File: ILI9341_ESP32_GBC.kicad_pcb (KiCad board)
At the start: 2 copper layers, 70 x 122.2 mm, 149 parts, among them CN2 PJ-3043-B, J1 USB_C_Receptacle_USB2.0_16P, J5 Micro_SD_Card_CD, J6 Conn_01x18_Socket, J7 Conn_01x32, Q10 XYC-PT204B-L1, Q2 BC817, Q3 BC817, Q5 PMOS, Q6 BC817, Q7 PMOS, Q8 PMOS, SW10 SW_Push, SW11 SW_Push, SW12 SW_Push, SW2 SW_Push, SW3 SW_Push, SW4 SW_Push, SW5 SW_Push, SW6 K3-1290S-J1, SW7 SW_Push, SW8 SW_Push, SW9 SW_Push, U1 CH340N, U11 ESP32-WROVER-E-N8R8, U2 XM5062S, U3 HT2348ARTZ8, U4 BQ25171QWDRCRQ1, U5 MCP23017_SO, U6 MCP23017_SO, U7 02FVS3, U8 PAM8406D, U9 TPS61028DRCR

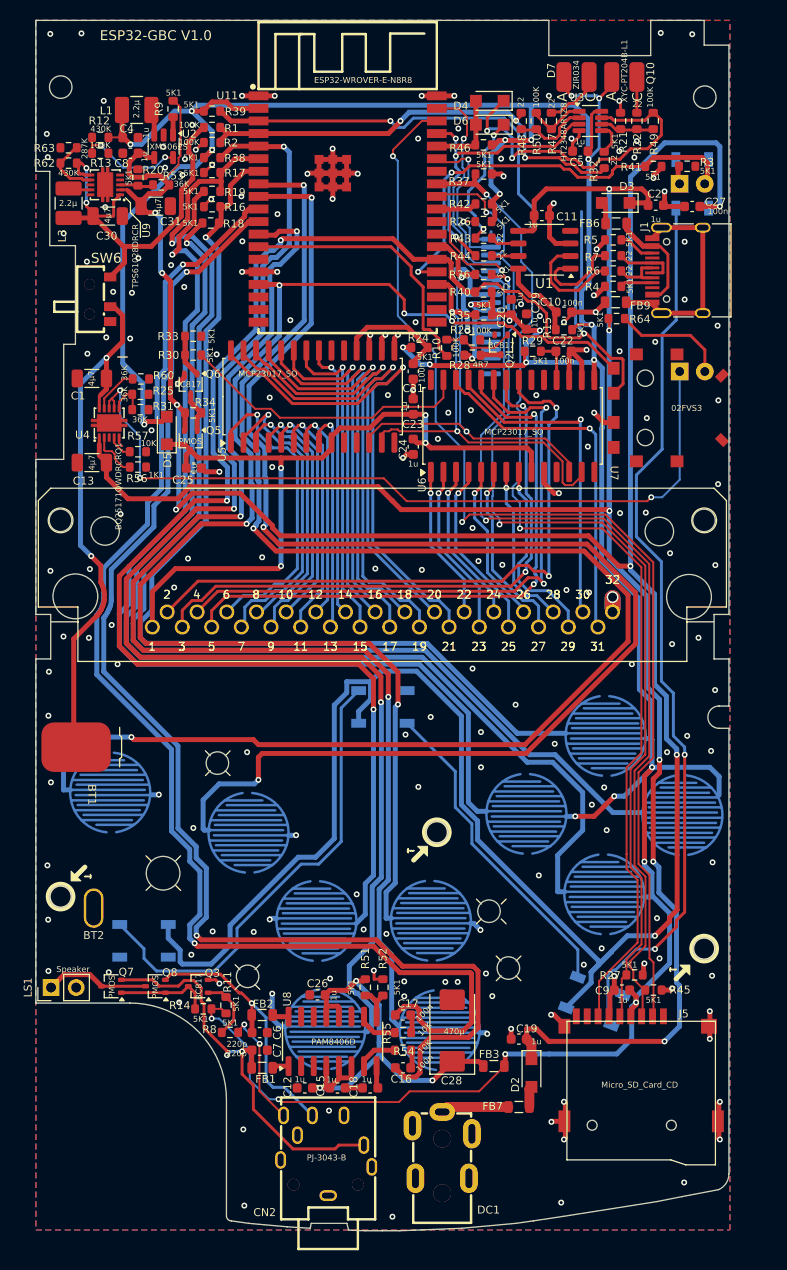
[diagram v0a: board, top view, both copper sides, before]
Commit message: update online version before change to esp32 s3
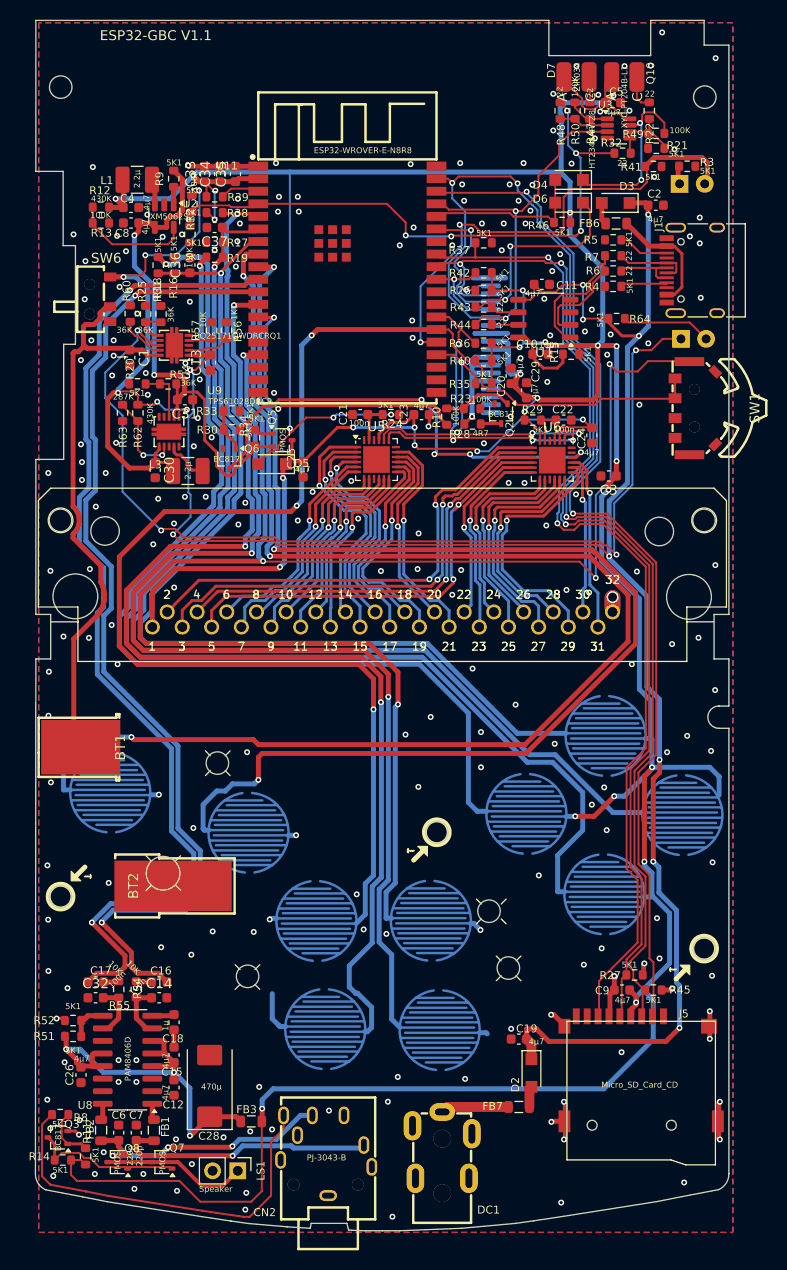
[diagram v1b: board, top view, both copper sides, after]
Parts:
- removed C27: 100n, Capacitor_SMD:C_0603_1608Metric
- removed D10, D11, D8, D9: WS2812B, LED_SMD:LED_WS2812B_PLCC4_5.0x5.0mm_P3.2mm
- removed FB9: FerriteBead_Small, Inductor_SMD:L_0805_2012Metric
- removed U7: 02FVS3, TheBrutzlers_Lib:02FVS3
- added C14: 220p, Capacitor_SMD:C_0603_1608Metric, F.Cu at (119.9, 135.8)
- added C3: 4µ7, Capacitor_SMD:C_0603_1608Metric, F.Cu at (165.3, 83.1)
- added C32: 220p, Capacitor_SMD:C_0603_1608Metric, F.Cu at (113.5, 135.8)
- added C33: 4µ7, Capacitor_SMD:C_0603_1608Metric, F.Cu at (124.5, 52.6)
- added C34: 4µ7, Capacitor_SMD:C_0603_1608Metric, F.Cu at (126.0, 52.6)
- added C35: 4µ7, Capacitor_SMD:C_0603_1608Metric, F.Cu at (127.6, 52.6)
- added C36: 220p, Capacitor_SMD:C_0603_1608Metric, F.Cu at (123.0, 61.8)
- added C37: 220p, Capacitor_SMD:C_0603_1608Metric, F.Cu at (125.5, 58.0)
- added SW1: TM-2023, easyeda2kicad:SW-SMD_TM-2023-1, F.Cu at (174.0, 76.2)
- BT1: footprint TheBrutzlers_Lib:BATTERY_AA_SMD_PLUS -> easyeda2kicad:CONN-SMD_MY-ZJ-3030
- BT2: footprint TheBrutzlers_Lib:NINTENDO_MINUS -> easyeda2kicad:BAT-SMD_MY-FJ-3031
- C1, C13, C30, C31: footprint Capacitor_SMD:C_1206_3216Metric -> Capacitor_SMD:C_0603_1608Metric
- C11, C12, C15, C19, C2, C20, C23, C24, C25, C26, C29, C4, C5, C8, C9: value 1u -> 4µ7
- C18: value 1u -> 1µ
- U5, U6: value MCP23017_SO -> AW9523B; footprint Package_SO:SOIC-28W_7.5x17.9mm_P1.27mm -> Package_DFN_QFN:QFN-24-1EP_4x4mm_P0.5mm_EP2.7x2.7mm
- moved R52 31.5 mm to (111.2, 138.1), turned to 180 degrees
- moved C17 31.2 mm to (113.5, 134.2)
- moved R51 29.9 mm to (111.2, 139.7), turned to 0 degrees
- moved L3 29.6 mm to (122.8, 82.6), turned to 0 degrees
- moved R55 29.0 mm to (115.8, 135.0), turned to -90 degrees
- moved R54 27.6 mm to (117.6, 135.0), turned to -90 degrees
- moved R63 27.3 mm to (116.2, 76.7), turned to -90 degrees
- moved LS1 26.4 mm to (127.8, 153.3), turned to -90 degrees
- moved R62 26.2 mm to (117.8, 76.7), turned to -90 degrees
- moved C16 26.1 mm to (119.9, 134.2), turned to 180 degrees
- moved C30 26.1 mm to (119.5, 82.5), turned to -90 degrees
- moved U9 25.7 mm to (120.9, 78.6), turned to -90 degrees
- moved C26 25.2 mm to (112.0, 143.6), turned to -90 degrees
- moved FB3 25.1 mm to (129.2, 148.3)
- moved C28 25.1 mm to (125.0, 144.7)
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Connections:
- C21 pad 2: Net-(U5-~{RESET}) -> Net-(U5-~{RST})
- C22 pad 2: Net-(U6-~{RESET}) -> Net-(U6-~{RST})
- J1 pad A1: Net-(J1-SHIELD) -> GND
- J1 pad A12: Net-(J1-SHIELD) -> GND
- J1 pad B1: Net-(J1-SHIELD) -> GND
- J1 pad B12: Net-(J1-SHIELD) -> GND
- J1 pad S1: Net-(J1-SHIELD) -> GND
- R24 pad 2: Net-(U5-~{RESET}) -> Net-(U5-~{RST})
- R29 pad 2: Net-(U6-~{RESET}) -> Net-(U6-~{RST})
- R30 pad 1: Net-(U6-GPA6) -> Net-(U6-P1_6)
- U5 pad 1: /DMG_CARD/CARD_A0 -> /DMG_CARD/CARD_A8
- U5 pad 10: GND -> /DMG_CARD/CARD_A4
- U5 pad 11: unconnected-(U5-NC-Pad11) -> /DMG_CARD/CARD_A5
- U5 pad 12: /I2C_CLK -> /DMG_CARD/CARD_A6
- U5 pad 13: /I2C_SDA -> /DMG_CARD/CARD_A7
- U5 pad 14: unconnected-(U5-NC-Pad14) -> /DMG_CARD/CARD_A12
- U5 pad 15: GND -> /DMG_CARD/CARD_A13
- U5 pad 16: GND -> /DMG_CARD/CARD_A14
- U5 pad 17: GND -> /DMG_CARD/CARD_A15
- U5 pad 18: Net-(U5-~{RESET}) -> GND
- U5 pad 19: unconnected-(U5-INTB-Pad19) -> /I2C_CLK
- U5 pad 2: /DMG_CARD/CARD_A1 -> /DMG_CARD/CARD_A9
- U5 pad 20: unconnected-(U5-INTA-Pad20) -> /I2C_SDA
- U5 pad 21: /DMG_CARD/CARD_A8 -> /DMG_CARD/CARD_VCC
- U5 pad 22: /DMG_CARD/CARD_A9 -> unconnected-(U5-~{INT}-Pad22)
- U5 pad 23: /DMG_CARD/CARD_A10 -> Net-(U5-~{RST})
- U5 pad 24: /DMG_CARD/CARD_A11 -> GND
- U5 pad 25: /DMG_CARD/CARD_A12 -> GND
- U5 pad 3: /DMG_CARD/CARD_A2 -> /DMG_CARD/CARD_A10
- U5 pad 4: /DMG_CARD/CARD_A3 -> /DMG_CARD/CARD_A11
- U5 pad 5: /DMG_CARD/CARD_A4 -> /DMG_CARD/CARD_A0
- U5 pad 6: /DMG_CARD/CARD_A5 -> /DMG_CARD/CARD_A1
- U5 pad 7: /DMG_CARD/CARD_A6 -> /DMG_CARD/CARD_A2
- U5 pad 8: /DMG_CARD/CARD_A7 -> /DMG_CARD/CARD_A3
- U5 pad 9: /DMG_CARD/CARD_VCC -> GND
- U6 pad 1: /DMG_CARD/CARD_D0 -> /DMG_CARD/CARD_CLK
- U6 pad 10: GND -> /DMG_CARD/CARD_D4
- U6 pad 11: unconnected-(U6-NC-Pad11) -> /DMG_CARD/CARD_D5
- U6 pad 12: /I2C_CLK -> /DMG_CARD/CARD_D6
- U6 pad 13: /I2C_SDA -> /DMG_CARD/CARD_D7
- U6 pad 14: unconnected-(U6-NC-Pad14) -> /DMG_CARD/CARD_~{RES}
- U6 pad 15: +3V3 -> /DMG_CARD/CARD_VIN
- U6 pad 16: GND -> Net-(U6-P1_6)
- U6 pad 17: GND -> unconnected-(U6-P1_7-Pad17)
- U6 pad 18: Net-(U6-~{RESET}) -> GND
- U6 pad 19: unconnected-(U6-INTB-Pad19) -> /I2C_CLK
- U6 pad 2: /DMG_CARD/CARD_D1 -> /DMG_CARD/CARD_~{WR}
- U6 pad 20: unconnected-(U6-INTA-Pad20) -> /I2C_SDA
- U6 pad 21: /DMG_CARD/CARD_CLK -> /DMG_CARD/CARD_VCC
- U6 pad 22: /DMG_CARD/CARD_~{WR} -> unconnected-(U6-~{INT}-Pad22)
- U6 pad 23: /DMG_CARD/CARD_~{RD} -> Net-(U6-~{RST})
- U6 pad 24: /DMG_CARD/CARD_~{CS} -> +3V3
- U6 pad 25: /DMG_CARD/CARD_~{RES} -> GND
- U6 pad 3: /DMG_CARD/CARD_D2 -> /DMG_CARD/CARD_~{RD}
- U6 pad 4: /DMG_CARD/CARD_D3 -> /DMG_CARD/CARD_~{CS}
- U6 pad 5: /DMG_CARD/CARD_D4 -> /DMG_CARD/CARD_D0
- U6 pad 6: /DMG_CARD/CARD_D5 -> /DMG_CARD/CARD_D1
- U6 pad 7: /DMG_CARD/CARD_D6 -> /DMG_CARD/CARD_D2
- U6 pad 8: /DMG_CARD/CARD_D7 -> /DMG_CARD/CARD_D3
- U6 pad 9: /DMG_CARD/CARD_VCC -> GND
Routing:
- net /V_BOOST: track 318.5 -> 53.2 mm, vias 8 -> 2
- net Net-(D8-DOUT): track 90.9 -> 0.00 mm, vias 2 -> 0
- net GND: track 138.1 -> 48.1 mm, vias 185 -> 216
- net Net-(D10-DOUT): track 47.5 -> 0.00 mm
- net Net-(U6-P1_6): track 0.00 -> 42.1 mm, vias 0 -> 4
- net /EN: track 40.4 -> 4.04 mm, vias 1 -> 0
- net Net-(D10-DIN): track 32.8 -> 0.00 mm
- net /SOUND_LEFT: track 132.8 -> 102.0 mm
- net /DMG_CARD/CARD_A15: track 53.1 -> 22.8 mm
- net Net-(U6-GPA6): track 29.7 -> 0.00 mm
- net /SPK_nEN: track 11.9 -> 39.9 mm, vias 2 -> 0
- net /SOUND_RIGHT: track 131.7 -> 103.7 mm
- net /DMG_CARD/CARD_A14: track 47.6 -> 19.6 mm
- net +3V3: track 371.6 -> 395.1 mm, vias 27 -> 25
- net /DMG_CARD/CARD_A13: track 47.1 -> 23.8 mm
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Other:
- outline, holes or cut-outs redrawn
- board text added: "ESP32-GBC V1.1"
- board text removed: "ESP32-GBC V1.0"

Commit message: updated version with esp32 s3 and i2s audio ic
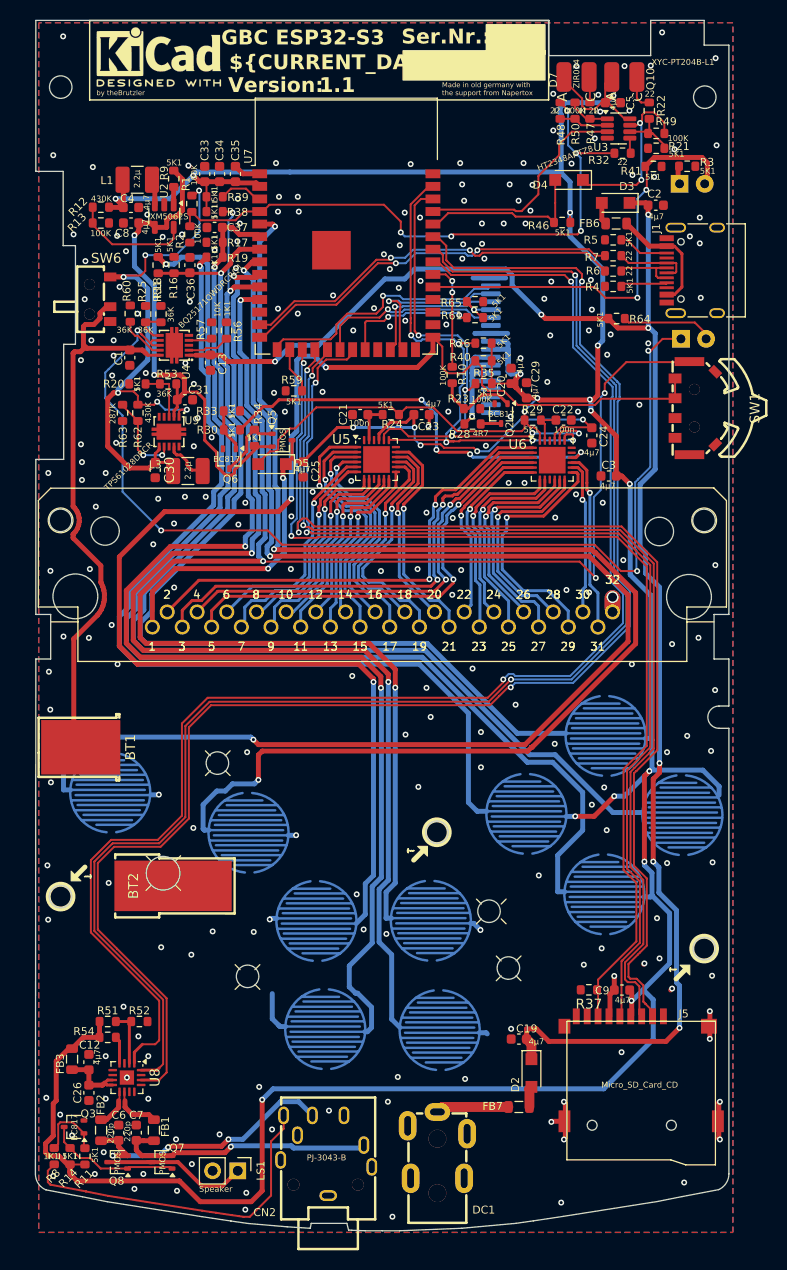
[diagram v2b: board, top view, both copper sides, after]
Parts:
- removed C10, C16, C17: 100n, Capacitor_SMD:C_0603_1608Metric
- removed C11, C15: 4µ7, Capacitor_SMD:C_0603_1608Metric
- removed C14, C32: 220p, Capacitor_SMD:C_0603_1608Metric
- removed C18: 1µ, Capacitor_SMD:C_0603_1608Metric
- removed C28: 470µ, Capacitor_Tantalum_SMD:CP_EIA-7343-43_Kemet-X
- removed D6: D, Diode_SMD:Nexperia_CFP3_SOD-123W
- removed R15, R26, R27, R42, R45: 5K1, Resistor_SMD:R_0603_1608Metric
- removed R43, R44: 22, Resistor_SMD:R_0603_1608Metric
- removed R55: 10K, Resistor_SMD:R_0603_1608Metric
- removed U1: CH340N, Package_SO:SOP-8_3.9x4.9mm_P1.27mm
- removed U11: ESP32-WROVER-E-N8R8, easyeda2kicad:WIFI-SMD_ESP32-WROVER-IE8MB
- added R59: 5K1, Resistor_SMD:R_0603_1608Metric, F.Cu at (133.5, 74.5)
- added R61: 5K1, Resistor_SMD:R_0603_1608Metric, F.Cu at (151.8, 67.1)
- added R65: 5K1, Resistor_SMD:R_0603_1608Metric, F.Cu at (151.8, 65.5)
- added REF**: , Symbol:KiCad-Logo2_5mm_SilkScreen, F.Cu at (119.9, 40.8)
- added U7: ESP32-WROOM-32, TheBrutzlers_Lib:ESP32-S3-WROOM-1, F.Cu at (138.8, 57.8)
- R54: value 10K -> 5K1
- R8: value 5K1 -> 1K1
- U8: value PAM8406D -> MAX98357AETE+T; footprint Package_SO:SOP-16_3.9x9.9mm_P1.27mm -> Package_DFN_QFN:QFN-16-1EP_3x3mm_P0.5mm_EP1.45x1.45mm
- moved R37 76.2 mm to (163.3, 135.0), turned to 180 degrees
- moved FB3 19.2 mm to (111.1, 142.0), turned to -90 degrees
- moved C12 8.98 mm to (112.8, 142.3), turned to 90 degrees
- moved R52 6.70 mm to (117.9, 138.2), turned to 0 degrees
- moved R54 5.64 mm to (114.7, 139.8), turned to 180 degrees
- moved R8 4.24 mm to (109.3, 151.8), turned to -90 degrees
- moved R10 4.24 mm to (149.5, 72.9), turned to -90 degrees
- moved R51 3.81 mm to (114.7, 138.2)
- moved C26 1.98 mm to (112.8, 145.4)
- moved Q3 1.95 mm to (111.3, 148.8)
- moved U8 1.80 mm to (116.6, 143.9), turned to -90 degrees
- moved R14 0.83 mm to (110.9, 151.8), turned to 90 degrees
- moved DC1 0.48 mm to (148.0, 150.7)
- moved R38 0.10 mm to (125.5, 56.4)
- moved R11 0.07 mm to (112.4, 151.8)
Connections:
- C12 pad 1: Net-(U8-PVDDL) -> Net-(C12-Pad1)
- C26 pad 1: Net-(U8-PVDDL) -> Net-(C12-Pad1)
- FB1 pad 1: Net-(U8-+OUT_L) -> Net-(U8-OUTN)
- FB2 pad 1: Net-(U8-+OUT_R) -> Net-(U8-OUTP)
- FB3 pad 2: Net-(U8-PVDDL) -> Net-(C12-Pad1)
- J5 pad 3: /MOSI -> /SD_MOSI
- J5 pad 5: /CLK -> /SD_CLK
- J6 pad 2: Net-(J6-Pin_2) -> /LCD_RESET
- J6 pad 3: /CLK -> /LCD_CLK
- J6 pad 6: /MOSI -> /LCD_MOSI
- R51 pad 1: Net-(U8-PVDDL) -> +3V3
- R51 pad 2: Net-(U8-MODE) -> Net-(U8-GAIN_SLOT)
- R52 pad 1: Net-(U8-MODE) -> Net-(U8-GAIN_SLOT)
- R54 pad 1: Net-(C16-Pad2) -> Net-(U8-SD_MODE)
- R54 pad 2: Net-(U8-INL) -> +3V3
- U8 pad 1: Net-(U8-+OUT_L) -> /I2S_DATA
- U8 pad 10: Net-(U8-INR) -> Net-(U8-OUTN)
- U8 pad 12: Net-(U8-PVDDL) -> (no net)
- U8 pad 13: Net-(U8-PVDDL) -> (no net)
- U8 pad 14: unconnected-(U8--OUT_R-Pad14) -> /I2S_WS
- U8 pad 16: Net-(U8-+OUT_R) -> /I2S_BCK
- U8 pad 2: GND -> Net-(U8-GAIN_SLOT)
- U8 pad 3: unconnected-(U8--OUT_L-Pad3) -> GND
- U8 pad 4: Net-(U8-PVDDL) -> Net-(U8-SD_MODE)
- U8 pad 5: Net-(U8-PVDDL) -> (no net)
- U8 pad 6: Net-(U8-PVDDL) -> (no net)
- U8 pad 7: Net-(U8-INL) -> Net-(C12-Pad1)
- U8 pad 8: Net-(U8-VREF) -> Net-(C12-Pad1)
- U8 pad 9: Net-(U8-MODE) -> Net-(U8-OUTP)
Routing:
- net /I2S_WS: track 0.00 -> 151.2 mm, vias 0 -> 2
- net /I2S_BCK: track 0.00 -> 148.3 mm, vias 0 -> 2
- net /I2S_DATA: track 0.00 -> 146.2 mm, vias 0 -> 2
- net /MOSI: track 124.0 -> 0.00 mm, vias 3 -> 0
- net /CLK: track 106.9 -> 0.00 mm, vias 3 -> 0
- net /SD_CLK: track 0.00 -> 105.8 mm, vias 0 -> 2
- net /SD_MOSI: track 0.00 -> 104.9 mm, vias 0 -> 2
- net /SOUND_RIGHT: track 103.7 -> 0.00 mm, vias 2 -> 0
- net /SOUND_LEFT: track 102.0 -> 0.00 mm, vias 2 -> 0
- net Net-(U8-PVDDL): track 42.5 -> 0.00 mm, vias 3 -> 0
- net /VUSB: track 195.8 -> 161.7 mm, vias 10 -> 7
- net /D-: track 9.65 -> 39.2 mm, vias 0 -> 2
- net /D+: track 12.9 -> 39.0 mm, vias 0 -> 2
- net /LCD_RESET: track 0.00 -> 26.0 mm, vias 0 -> 1
- net +3V3: track 395.1 -> 371.6 mm, vias 25 -> 17
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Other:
- board text added: "${CURRENT_DATE}"
- board text added: "1.1"
- board text added: "GBC ESP32-S3"
- board text added: "Made in old germany with the support from Napertox"
- board text added: "Ser.Nr.:"
- board text added: "Version:"
- board text added: "by theBrutzler"
- board text removed: "ESP32-GBC V1.1"

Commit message: Order V1
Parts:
- removed C21, C22: 100n, Capacitor_SMD:C_0603_1608Metric
- removed C23, C24, C25: 4µ7, Capacitor_SMD:C_0603_1608Metric
- removed CN2: PJ-3043-B, easyeda2kicad:AUDIO-TH_PJ-3043-B
- removed J7: Conn_01x32, TheBrutzlers_Lib:DMG_01_CARDRIDGE_CONNECTOR
- removed Q3, Q6: BC817, Package_TO_SOT_SMD:SOT-323_SC-70
- removed Q5, Q7, Q8: PMOS, Package_TO_SOT_SMD:SOT-323_SC-70
- removed R29, R30, R33, R34, R41: 5K1, Resistor_SMD:R_0603_1608Metric
- removed R32: 22, Resistor_SMD:R_0603_1608Metric
- removed R56: 1K1, Resistor_SMD:R_0603_1608Metric
- removed U5, U6: AW9523B, Package_DFN_QFN:QFN-24-1EP_4x4mm_P0.5mm_EP2.7x2.7mm
- added Audio1: PJ-3537-X, easyeda2kicad:AUDIO-SMD_PJ-3420-A-SMT_C319102, F.Cu at (136.9, 152.4)
- added CN1: KH-CL0.5-H2.0-18PS, easyeda2kicad:FPC-SMD_KH-CL0.5-H2.0-18PS, B.Cu at (136.3, 61.3)
- added FPC1: 0.8K-BS-18PWB(H=2.0), easyeda2kicad:FPC-SMD_18P-P0.80_HDGC_0.8K-BS-18PWB, B.Cu at (153.4, 61.2)
- added G***: LOGO, TheBrutzlers_Lib:Platinenmacher_14, F.Cu at (152.6, 49.3)
- added J2: Conn_01x05_Pin, Connector_PinHeader_2.54mm:PinHeader_1x05_P2.54mm_Vertical, F.Cu at (137.3, 82.4)
- added R15: 1K1, Resistor_SMD:R_0603_1608Metric, F.Cu at (166.4, 46.2)
- added R26: 5K1, Resistor_SMD:R_0603_1608Metric, F.Cu at (145.1, 72.9)
- added REF**: OSHW-Logo2_7.3x6mm_SilkScreen, Symbol:OSHW-Logo2_7.3x6mm_SilkScreen, F.Cu at (116.0, 48.2)
- added SM3: SYM_Arrow45_Tiny, TheBrutzlers_Lib:Symbol_kurzschlussblog, F.Cu at (119.6, 50.0)
- D14: footprint LED_THT:LED_D3.0mm_FlatTop -> LED_SMD:LED_0603_1608Metric; moved to F.Cu
- D5: value D -> LED; footprint Diode_SMD:Nexperia_CFP3_SOD-123W -> LED_SMD:LED_0603_1608Metric; moved to B.Cu
- R11, R14, R20, R21, R24: value 5K1 -> 1K1
- R48: value 22 -> 1K1
- R53: value 36K -> 10K
- R8: value 1K1 -> 5K1
- SW2, SW3, SW4, SW5: footprint TheBrutzlers_Lib:RubberpadButton_250µ_250µ -> TheBrutzlers_Lib:RubberpadButton_GBC_CROSS
- U3: value HT2348ARTZ8 -> LM358LVIDDFR
- U7: value ESP32-WROOM-32 -> ESP32-S3-WROOM-1-N16R8
- moved R14 120.0 mm to (167.9, 46.2)
- moved R8 105.7 mm to (151.8, 55.0), turned to 0 degrees
- moved R11 84.6 mm to (126.8, 68.4)
- moved D5 50.2 mm to (173.7, 55.1), turned to 0 degrees
- moved R24 34.0 mm to (166.6, 52.1), turned to 0 degrees
- moved R28 12.9 mm to (152.8, 65.0)
- moved Q2 9.81 mm to (153.0, 67.1), turned to 0 degrees
- moved R23 8.78 mm to (150.3, 67.6), turned to -90 degrees
- moved J6 8.70 mm to (153.4, 61.2)
- moved R10 8.44 mm to (150.3, 64.5)
- moved C20 8.06 mm to (156.5, 65.0), turned to 0 degrees
- moved C29 7.87 mm to (156.5, 66.6), turned to 0 degrees
- moved R61 7.80 mm to (151.8, 59.3)
- moved R65 7.80 mm to (151.8, 57.7)
- moved R49 6.19 mm to (166.6, 53.6), turned to 180 degrees
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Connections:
- D5 pad 1: /DMG_CARD/CARD_VCC -> Net-(D1-K)
- D5 pad 2: +3V3 -> /LED
- J6 pad 15: unconnected-(J6-Pin_15-Pad15) -> Net-(J6-Pin_15)
- J6 pad 16: unconnected-(J6-Pin_16-Pad16) -> Net-(J6-Pin_16)
- J6 pad 17: unconnected-(J6-Pin_17-Pad17) -> Net-(J6-Pin_17)
- J6 pad 18: unconnected-(J6-Pin_18-Pad18) -> Net-(J6-Pin_18)
- J6 pad 7: unconnected-(J6-Pin_7-Pad7) -> Net-(J6-Pin_7)
- LS1 pad 2: GND -> Net-(Audio1-Pad6)
- R11 pad 1: +3V3 -> Net-(U4-ISET)
- R11 pad 2: Net-(Q3-B) -> GND
- R14 pad 1: +3V3 -> Net-(R14-Pad1)
- R14 pad 2: Net-(Q3-C) -> Net-(Q10-E)
- R24 pad 1: +3V3 -> /V_BAT_ADC
- R24 pad 2: Net-(U5-~{RST}) -> Net-(U3B-+)
- R40 pad 1: /KEY_OPTION -> /KEY_BOOT
- R48 pad 1: Net-(U3A--) -> Net-(U3A-+)
- R48 pad 2: /V_BAT_ADC -> /TXD
- R49 pad 1: Net-(U3B--) -> Net-(U3B-+)
- R50 pad 2: Net-(U3A--) -> Net-(U3A-+)
- R8 pad 1: Net-(Q3-B) -> /LCD_RESET
- R8 pad 2: /SPK_nEN -> +3V3
- SW1 pad 2: GND -> /KEY_MENU
- SW1 pad 3: /KEY_MENU -> GND
- SW1 pad 4: unconnected-(SW1-Pad4) -> GND
- SW1 pad 6: unconnected-(SW1-Pad6) -> GND
- SW1 pad C: /KEY_OPTION -> GND
- SW1 pad T: GND -> /KEY_BOOT
- SW5 pad 1: +3V3 -> /KEY_DOWN
- SW5 pad 2: /KEY_DOWN -> +3V3
- U3 pad 2: Net-(U3A--) -> /V_BAT_ADC
- U3 pad 3: /TXD -> Net-(U3A-+)
- U7 pad 12: unconnected-(U7-IO8-Pad12) -> /KEY_OPTION
- U7 pad 26: unconnected-(U7-IO45-Pad26) -> Net-(U7-IO45)
- U7 pad 27: /KEY_OPTION -> /KEY_BOOT
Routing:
- net /DMG_CARD/CARD_VCC: track 76.7 -> 0.00 mm, vias 7 -> 0
- net /DMG_CARD/CARD_~{WR}: track 48.5 -> 0.00 mm, vias 2 -> 0
- net /DMG_CARD/CARD_CLK: track 48.3 -> 0.00 mm, vias 2 -> 0
- net /DMG_CARD/CARD_~{CS}: track 45.5 -> 0.00 mm, vias 2 -> 0
- net /DMG_CARD/CARD_~{RD}: track 45.2 -> 0.00 mm, vias 2 -> 0
- net Net-(U6-P1_6): track 41.6 -> 0.00 mm, vias 4 -> 0
- net /SPK_nEN: track 34.5 -> 0.00 mm
- net /KEY_BOOT: track 0.00 -> 31.3 mm
- net /KEY_OPTION: track 145.2 -> 115.8 mm, vias 3 -> 6
- net Net-(Audio1-Pad6): track 0.00 -> 26.1 mm
- net /DMG_CARD/CARD_D7: track 25.7 -> 0.00 mm, vias 1 -> 0
- net /DMG_CARD/CARD_A9: track 25.1 -> 0.00 mm, vias 1 -> 0
- net +3V3: track 371.6 -> 396.1 mm
- net /DMG_CARD/CARD_A11: track 24.2 -> 0.00 mm, vias 1 -> 0
- net /DMG_CARD/CARD_A8: track 24.0 -> 0.00 mm, vias 1 -> 0
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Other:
- outline, holes or cut-outs redrawn
- board text added: "1.2"
- board text added: "22"
- board text added: "realSixi ist immer erstererer PunishTheRookie WodoWiesel milchmann Napertox wichtiger mod <3 Antrafox pinqin_th Tomekk20 noch_online lieblings mod :* der_Digga meins_da Naegolus HeroAAX yeTTizTV rsger12 Schattenwelt Opel_Calibra_16V Schnullerin Schnuller"
- board text removed: "1.1"
